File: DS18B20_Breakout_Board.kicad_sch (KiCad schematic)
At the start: 4 parts, among them J1 Conn_01x03_Socket, J2 Conn_01x03_Socket, U2 DS18B20

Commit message: Attached part number to components.
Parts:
- J1: footprint Connector_PinSocket_2.54mm:PinSocket_1x03_P2.54mm_Vertical -> Connector_USB:USB_C_Receptacle_G-Switch_GT-USB-7010ASV; LCSC PN (none) -> C2988369
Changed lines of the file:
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@@
 			)
 		)
-		(property "Footprint" "Connector_PinSocket_2.54mm:PinSocket_1x03_P2.54mm_Vertical"
+		(property "Footprint" "Connector_USB:USB_C_Receptacle_G-Switch_GT-USB-7010ASV"
 			(at 187.96 91.44 0)
 			(hide yes)
@@
 			(at 187.96 91.44 0)
 			(hide yes)
+			(show_name no)
+			(do_not_autoplace no)
+			(effects
+				(font
+					(size 1.27 1.27)
+				)
+			)
+		)
+		(property "LCSC PN" "C2988369"
+			(at 187.96 91.44 0)
+			(hide yes)

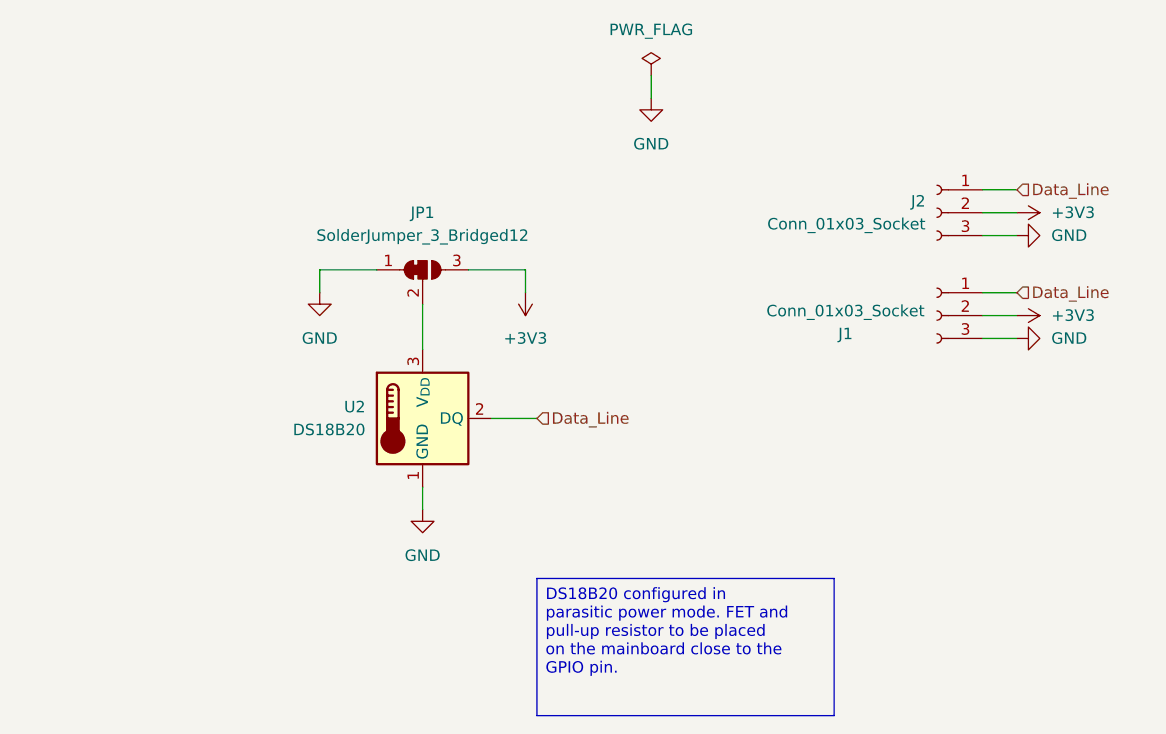
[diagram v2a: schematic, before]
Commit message: Fix ERC errors.
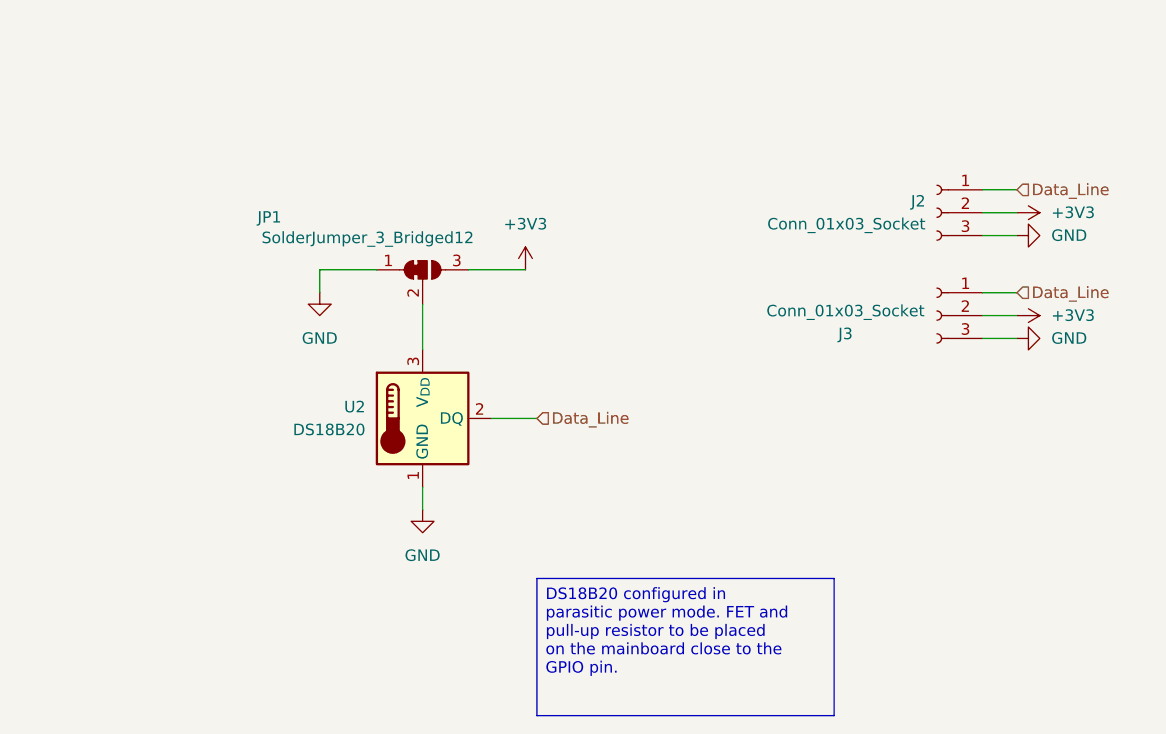
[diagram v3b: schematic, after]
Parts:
- renumbered J1 to J3
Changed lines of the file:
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@@
 	(wire
 		(pts
-			(xy 156.21 64.77) (xy 156.21 67.31)
+			(xy 193.04 77.47) (xy 196.85 77.47)
 		)
 		(stroke
@@
 	(wire
 		(pts
-			(xy 193.04 77.47) (xy 196.85 77.47)
+			(xy 125.73 86.36) (xy 119.38 86.36)
 		)
 		(stroke
@@
 	(wire
 		(pts
-			(xy 125.73 86.36) (xy 119.38 86.36)
+			(xy 138.43 102.87) (xy 143.51 102.87)
 		)
 		(stroke
@@
 	(wire
 		(pts
-			(xy 138.43 102.87) (xy 143.51 102.87)
+			(xy 193.04 82.55) (xy 196.85 82.55)
 		)
 		(stroke
@@
 	(wire
 		(pts
-			(xy 193.04 82.55) (xy 196.85 82.55)
+			(xy 193.04 93.98) (xy 196.85 93.98)
 		)
 		(stroke
@@
 	(wire
 		(pts
-			(xy 193.04 93.98) (xy 196.85 93.98)
-		)
-		(stroke
-			(width 0)
-			(type default)
-		)
-	)
-	(wire
-		(pts
 			(xy 193.04 91.44) (xy 196.85 91.44)
-		)
-		(stroke
-			(width 0)
-			(type default)
-		)
-	)
-	(wire
-		(pts
-			(xy 142.24 86.36) (xy 142.24 88.9)
 		)
 		(stroke
@@
 		(in_pos_files yes)
 		(dnp no)
-		(fields_autoplaced yes)
 		(property "Reference" "JP1"
-			(at 130.81 80.01 0)
+			(at 113.792 80.518 0)
 			(show_name no)
 			(do_not_autoplace no)
@@
 		)
 		(property "Value" "SolderJumper_3_Bridged12"
-			(at 130.81 82.55 0)
+			(at 124.714 82.804 0)
 			(show_name no)
 			(do_not_autoplace no)
@@
 				(path "/d4589ebf-bd63-493c-aca1-d4527007b8a8"
 					(reference "JP1")
+					(unit 1)
+				)
+			)
+		)
+	)
+	(symbol
+		(lib_id "power:+3V3")
+		(at 142.24 86.36 0)
+		(unit 1)
+		(body_style 1)
+		(exclude_from_sim no)
+		(in_bom yes)
+		(on_board yes)
+		(in_pos_files yes)
+		(dnp no)
+		(fields_autoplaced yes)
+		(property "Reference" "#PWR044"
+			(at 142.24 90.17 0)
+			(hide yes)
+			(show_name no)
+			(do_not_autoplace no)
+			(effects
+				(font
+					(size 1.27 1.27)
+				)
+			)
+		)
+		(property "Value" "+3V3"
+			(at 142.24 81.28 0)
+			(show_name no)
+			(do_not_autoplace no)
+			(effects
+				(font
+					(size 1.27 1.27)
+				)
+			)
+		)
+		(property "Footprint" ""
+			(at 142.24 86.36 0)
+			(hide yes)
+			(show_name no)
+			(do_not_autoplace no)
+			(effects
+				(font
+					(size 1.27 1.27)
+				)
+			)
+		)
+		(property "Datasheet" ""
+			(at 142.24 86.36 0)
+			(hide yes)
+			(show_name no)
+			(do_not_autoplace no)
+			(effects
+				(font
+					(size 1.27 1.27)
+				)
+			)
+		)
+		(property "Description" "Power symbol creates a global label with name \"+3V3\""
+			(at 142.24 86.36 0)
+			(hide yes)
+			(show_name no)
+			(do_not_autoplace no)
+			(effects
+				(font
+					(size 1.27 1.27)
+				)
+			)
+		)
+		(pin "1"
+		)
+		(instances
+			(project "CC3501-project-hardware"
+				(path "/4a2d49bb-8ba4-4c60-a8f0-05b8d2544445/0bf64f49-ae63-4b77-9d9b-174c7658c64d"
+					(reference "#PWR044")
 					(unit 1)
 				)
@@
 	)
 	(symbol
-		(lib_id "power:PWR_FLAG")
-		(at 156.21 64.77 0)
-		(unit 1)
-		(body_style 1)
-		(exclude_from_sim no)
-		(in_bom yes)
-		(on_board yes)
-		(in_pos_files yes)
-		(dnp no)
-		(fields_autoplaced yes)
-		(property "Reference" "#FLG01"
-			(at 156.21 62.865 0)
-			(hide yes)
-			(show_name no)
-			(do_not_autoplace no)
-			(effects
-				(font
-					(size 1.27 1.27)
-				)
-			)
-		)
-		(property "Value" "PWR_FLAG"
-			(at 156.21 59.69 0)
-			(show_name no)
-			(do_not_autoplace no)
-			(effects
-				(font
-					(size 1.27 1.27)
-				)
-			)
-		)
-		(property "Footprint" ""
-			(at 156.21 64.77 0)
-			(hide yes)
-			(show_name no)
-			(do_not_autoplace no)
-			(effects
-				(font
-					(size 1.27 1.27)
-				)
-			)
-		)
-		(property "Datasheet" ""
-			(at 156.21 64.77 0)
-			(hide yes)
-			(show_name no)
-			(do_not_autoplace no)
-			(effects
-				(font
-					(size 1.27 1.27)
-				)
-			)
-		)
-		(property "Description" "Special symbol for telling ERC where power comes from"
-			(at 156.21 64.77 0)
-			(hide yes)
-			(show_name no)
-			(do_not_autoplace no)
-			(effects
-				(font
-					(size 1.27 1.27)
-				)
-			)
-		)
-		(pin "1"
-		)
-		(instances
-			(project "CC3501-project-hardware"
-				(path "/4a2d49bb-8ba4-4c60-a8f0-05b8d2544445/0bf64f49-ae63-4b77-9d9b-174c7658c64d"
-					(reference "#FLG01")
-					(unit 1)
-				)
-			)
-			(project "DS18B20 Breakout Board"
-				(path "/d4589ebf-bd63-493c-aca1-d4527007b8a8"
-					(reference "#FLG01")
-					(unit 1)
-				)
-			)
-		)
-	)
-	(symbol
 		(lib_id "Connector:Conn_01x03_Socket")
 		(at 187.96 91.44 0)
@@
 		(in_pos_files yes)
 		(dnp no)
-		(property "Reference" "J1"
+		(property "Reference" "J3"
 			(at 177.8 93.472 0)
 			(show_name no)
@@
 			(project "CC3501-project-hardware"
 				(path "/4a2d49bb-8ba4-4c60-a8f0-05b8d2544445/0bf64f49-ae63-4b77-9d9b-174c7658c64d"
-					(reference "J1")
+					(reference "J3")
 					(unit 1)
 				)
@@
 	(symbol
 		(lib_id "power:+3V3")
-		(at 142.24 88.9 180)
-		(unit 1)
-		(body_style 1)
-		(exclude_from_sim no)
-		(in_bom yes)
-		(on_board yes)
-		(in_pos_files yes)
-		(dnp no)
-		(fields_autoplaced yes)
-		(property "Reference" "#PWR08"
-			(at 142.24 85.09 0)
-			(hide yes)
-			(show_name no)
-			(do_not_autoplace no)
-			(effects
-				(font
-					(size 1.27 1.27)
-				)
-			)
-		)
-		(property "Value" "+3V3"
-			(at 142.24 93.98 0)
-			(show_name no)
-			(do_not_autoplace no)
-			(effects
-				(font
-					(size 1.27 1.27)
-				)
-			)
-		)
-		(property "Footprint" ""
-			(at 142.24 88.9 0)
-			(hide yes)
-			(show_name no)
-			(do_not_autoplace no)
-			(effects
-				(font
-					(size 1.27 1.27)
-				)
-			)
-		)
-		(property "Datasheet" ""
-			(at 142.24 88.9 0)
-			(hide yes)
-			(show_name no)
-			(do_not_autoplace no)
-			(effects
-				(font
-					(size 1.27 1.27)
-				)
-			)
-		)
-		(property "Description" "Power symbol creates a global label with name \"+3V3\""
-			(at 142.24 88.9 0)
-			(hide yes)
-			(show_name no)
-			(do_not_autoplace no)
-			(effects
-				(font
-					(size 1.27 1.27)
-				)
-			)
-		)
-		(pin "1"
-		)
-		(instances
-			(project "CC3501-project-hardware"
-				(path "/4a2d49bb-8ba4-4c60-a8f0-05b8d2544445/0bf64f49-ae63-4b77-9d9b-174c7658c64d"
-					(reference "#PWR08")
-					(unit 1)
-				)
-			)
-			(project "DS18B20 Breakout Board"
-				(path "/d4589ebf-bd63-493c-aca1-d4527007b8a8"
-					(reference "#PWR08")
-					(unit 1)
-				)
-			)
-		)
-	)
-	(symbol
-		(lib_id "power:GND")
-		(at 156.21 67.31 0)
-		(unit 1)
-		(body_style 1)
-		(exclude_from_sim no)
-		(in_bom yes)
-		(on_board yes)
-		(in_pos_files yes)
-		(dnp no)
-		(fields_autoplaced yes)
-		(property "Reference" "#PWR01"
-			(at 156.21 73.66 0)
-			(hide yes)
-			(show_name no)
-			(do_not_autoplace no)
-			(effects
-				(font
-					(size 1.27 1.27)
-				)
-			)
-		)
-		(property "Value" "GND"
-			(at 156.21 72.39 0)
-			(show_name no)
-			(do_not_autoplace no)
-			(effects
-				(font
-					(size 1.27 1.27)
-				)
-			)
-		)
-		(property "Footprint" ""
-			(at 156.21 67.31 0)
-			(hide yes)
-			(show_name no)
-			(do_not_autoplace no)
-			(effects
-				(font
-					(size 1.27 1.27)
-				)
-			)
-		)
-		(property "Datasheet" ""
-			(at 156.21 67.31 0)
-			(hide yes)
-			(show_name no)
-			(do_not_autoplace no)
-			(effects
-				(font
-					(size 1.27 1.27)
-				)
-			)
-		)
-		(property "Description" "Power symbol creates a global label with name \"GND\" , ground"
-			(at 156.21 67.31 0)
-			(hide yes)
-			(show_name no)
-			(do_not_autoplace no)
-			(effects
-				(font
-					(size 1.27 1.27)
-				)
-			)
-		)
-		(pin "1"
-		)
-		(instances
-			(project "CC3501-project-hardware"
-				(path "/4a2d49bb-8ba4-4c60-a8f0-05b8d2544445/0bf64f49-ae63-4b77-9d9b-174c7658c64d"
-					(reference "#PWR01")
-					(unit 1)
-				)
-			)
-			(project "DS18B20 Breakout Board"
-				(path "/d4589ebf-bd63-493c-aca1-d4527007b8a8"
-					(reference "#PWR01")
-					(unit 1)
-				)
-			)
-		)
-	)
-	(symbol
-		(lib_id "power:+3V3")
 		(at 196.85 80.01 270)
 		(unit 1)
@@
 		(dnp no)
 		(fields_autoplaced yes)
-		(property "Reference" "#PWR06"
+		(property "Reference" "#PWR075"
 			(at 193.04 80.01 0)
 			(hide yes)
@@
 			(project "CC3501-project-hardware"
 				(path "/4a2d49bb-8ba4-4c60-a8f0-05b8d2544445/0bf64f49-ae63-4b77-9d9b-174c7658c64d"
-					(reference "#PWR06")
-					(unit 1)
-				)
-			)
-			(project "DS18B20 Breakout Board"
-				(path "/d4589ebf-bd63-493c-aca1-d4527007b8a8"
-					(reference "#PWR06")
-					(unit 1)
-				)
+					(reference "#PWR075")
+					(unit 1)
+				)

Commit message: Remove duplicated power flag.
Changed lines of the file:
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@@
 	(wire
 		(pts
-			(xy 125.73 86.36) (xy 119.38 86.36)
+			(xy 138.43 102.87) (xy 143.51 102.87)
 		)
 		(stroke
@@
 	(wire
 		(pts
-			(xy 138.43 102.87) (xy 143.51 102.87)
+			(xy 193.04 82.55) (xy 196.85 82.55)
 		)
 		(stroke
@@
 	(wire
 		(pts
-			(xy 193.04 82.55) (xy 196.85 82.55)
+			(xy 193.04 93.98) (xy 196.85 93.98)
 		)
 		(stroke
@@
 	(wire
 		(pts
-			(xy 193.04 93.98) (xy 196.85 93.98)
+			(xy 193.04 91.44) (xy 196.85 91.44)
 		)
 		(stroke
@@
 	(wire
 		(pts
-			(xy 193.04 91.44) (xy 196.85 91.44)
+			(xy 119.38 86.36) (xy 125.73 86.36)
 		)
 		(stroke
@@
 	)
 	(symbol
+		(lib_id "power:GND")
+		(at 119.38 88.9 0)
+		(unit 1)
+		(body_style 1)
+		(exclude_from_sim no)
+		(in_bom yes)
+		(on_board yes)
+		(in_pos_files yes)
+		(dnp no)
+		(fields_autoplaced yes)
+		(property "Reference" "#PWR04"
+			(at 119.38 95.25 0)
+			(hide yes)
+			(show_name no)
+			(do_not_autoplace no)
+			(effects
+				(font
+					(size 1.27 1.27)
+				)
+			)
+		)
+		(property "Value" "GND"
+			(at 119.38 93.98 0)
+			(show_name no)
+			(do_not_autoplace no)
+			(effects
+				(font
+					(size 1.27 1.27)
+				)
+			)
+		)
+		(property "Footprint" ""
+			(at 119.38 88.9 0)
+			(hide yes)
+			(show_name no)
+			(do_not_autoplace no)
+			(effects
+				(font
+					(size 1.27 1.27)
+				)
+			)
+		)
+		(property "Datasheet" ""
+			(at 119.38 88.9 0)
+			(hide yes)
+			(show_name no)
+			(do_not_autoplace no)
+			(effects
+				(font
+					(size 1.27 1.27)
+				)
+			)
+		)
+		(property "Description" "Power symbol creates a global label with name \"GND\" , ground"
+			(at 119.38 88.9 0)
+			(hide yes)
+			(show_name no)
+			(do_not_autoplace no)
+			(effects
+				(font
+					(size 1.27 1.27)
+				)
+			)
+		)
+		(pin "1"
+		)
+		(instances
+			(project "CC3501-project-hardware"
+				(path "/4a2d49bb-8ba4-4c60-a8f0-05b8d2544445/0bf64f49-ae63-4b77-9d9b-174c7658c64d"
+					(reference "#PWR04")
+					(unit 1)
+				)
+			)
+		)
+	)
+	(symbol
 		(lib_id "Connector:Conn_01x03_Socket")
 		(at 187.96 91.44 0)
@@
 					(unit 1)
 				)
-			)
-		)
-	)
-	(symbol
-		(lib_id "power:GND")
-		(at 119.38 88.9 0)
-		(unit 1)
-		(body_style 1)
-		(exclude_from_sim no)
-		(in_bom yes)
-		(on_board yes)
-		(in_pos_files yes)
-		(dnp no)
-		(fields_autoplaced yes)
-		(property "Reference" "#PWR04"
-			(at 119.38 95.25 0)
-			(hide yes)
-			(show_name no)
-			(do_not_autoplace no)
-			(effects
-				(font
-					(size 1.27 1.27)
-				)
-			)
-		)
-		(property "Value" "GND"
-			(at 119.38 93.98 0)
-			(show_name no)
-			(do_not_autoplace no)
-			(effects
-				(font
-					(size 1.27 1.27)
-				)
-			)
-		)
-		(property "Footprint" ""
-			(at 119.38 88.9 0)
-			(hide yes)
-			(show_name no)
-			(do_not_autoplace no)
-			(effects
-				(font
-					(size 1.27 1.27)
-				)
-			)
-		)
-		(property "Datasheet" ""
-			(at 119.38 88.9 0)
-			(hide yes)
-			(show_name no)
-			(do_not_autoplace no)
-			(effects
-				(font
-					(size 1.27 1.27)
-				)
-			)
-		)
-		(property "Description" "Power symbol creates a global label with name \"GND\" , ground"
-			(at 119.38 88.9 0)
-			(hide yes)
-			(show_name no)
-			(do_not_autoplace no)
-			(effects
-				(font
-					(size 1.27 1.27)
-				)
-			)
-		)
-		(pin "1"
-		)
-		(instances
-			(project "CC3501-project-hardware"
-				(path "/4a2d49bb-8ba4-4c60-a8f0-05b8d2544445/0bf64f49-ae63-4b77-9d9b-174c7658c64d"
-					(reference "#PWR04")
-					(unit 1)
-				)
-			)
-			(project "DS18B20 Breakout Board"
-				(path "/d4589ebf-bd63-493c-aca1-d4527007b8a8"
-					(reference "#PWR04")
-					(unit 1)
-				)

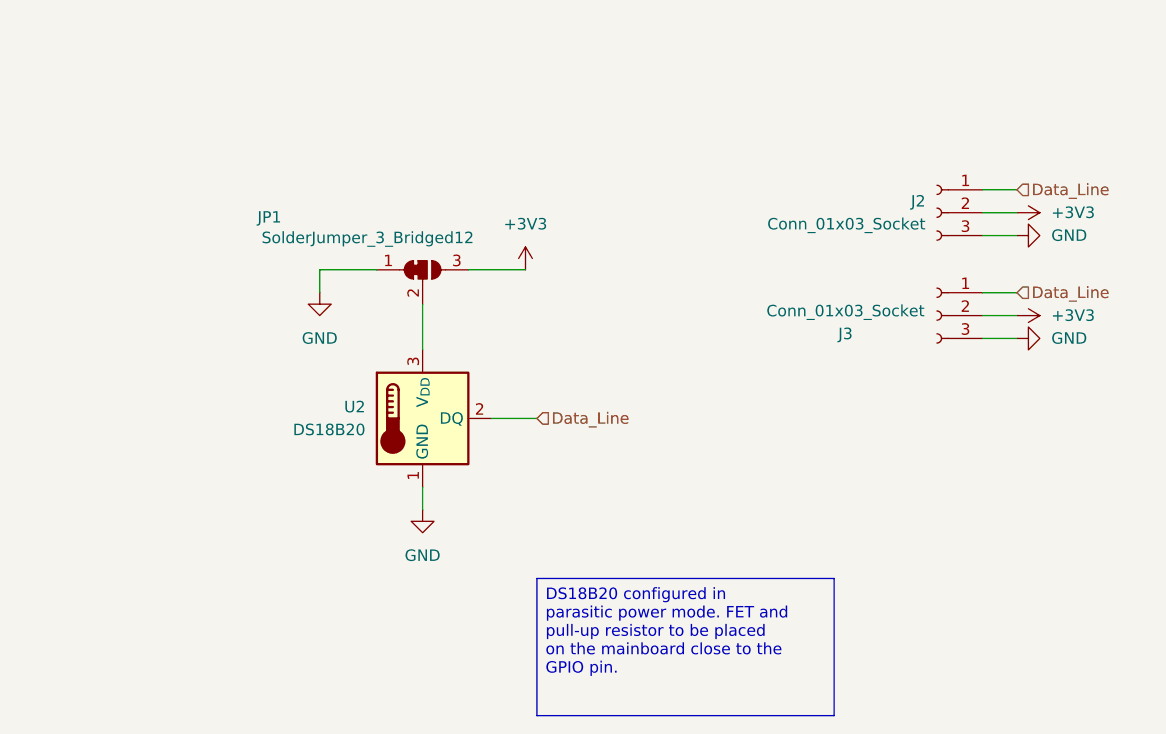
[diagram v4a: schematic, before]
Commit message: Change wiring on temp sensor.
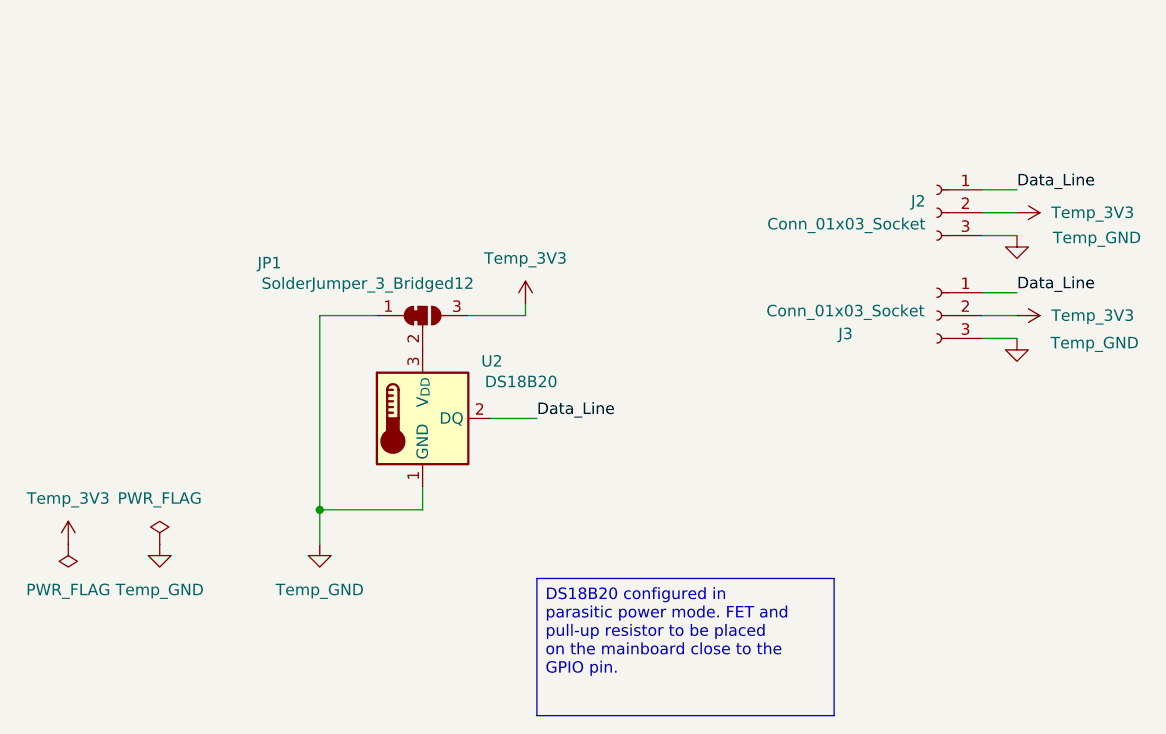
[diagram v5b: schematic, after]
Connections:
- net +3V3 renamed Temp_3V3
- net GND renamed Temp_GND
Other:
- moved on the sheet: JP1

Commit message: Rewire TFT display to power with 5V and allowing backlight switching via FET.
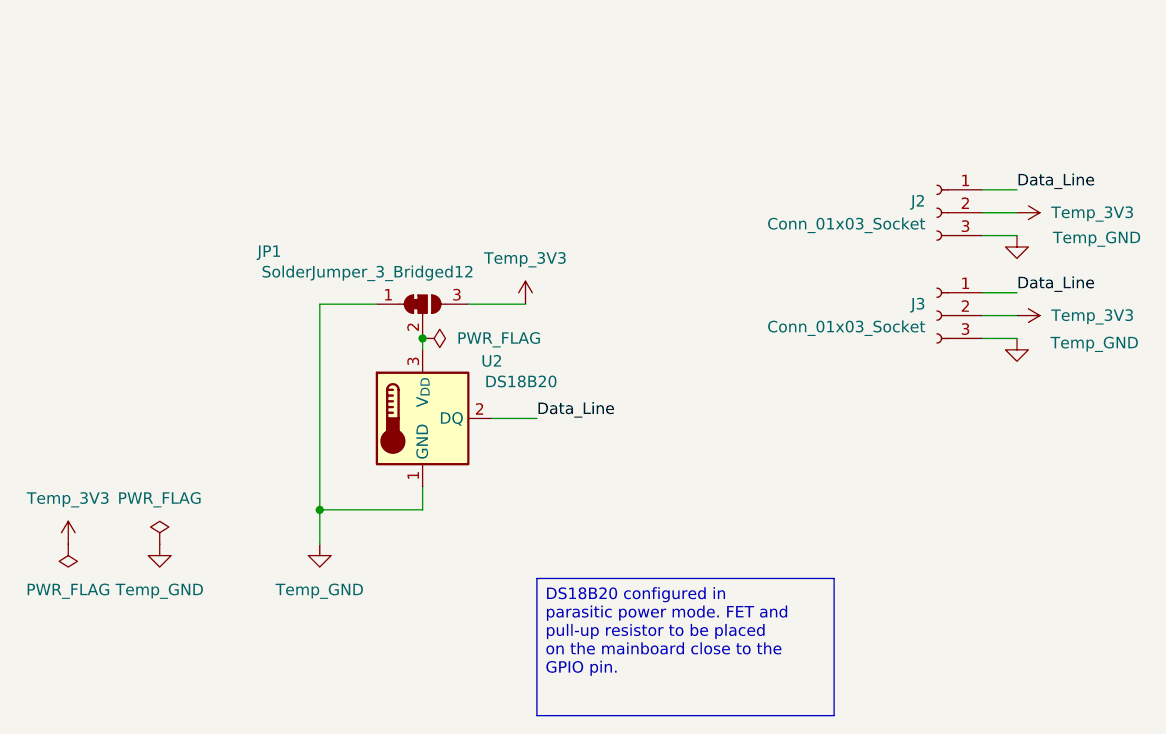
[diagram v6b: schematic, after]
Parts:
- J3: footprint Connector_USB:USB_C_Receptacle_G-Switch_GT-USB-7010ASV -> Connector_PinSocket_2.54mm:PinSocket_1x03_P2.54mm_Vertical; LCSC PN C2988369 -> (none)
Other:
- moved on the sheet: JP1
